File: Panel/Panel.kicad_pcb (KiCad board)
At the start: 2 copper layers, 30 x 128.5 mm, 7 parts

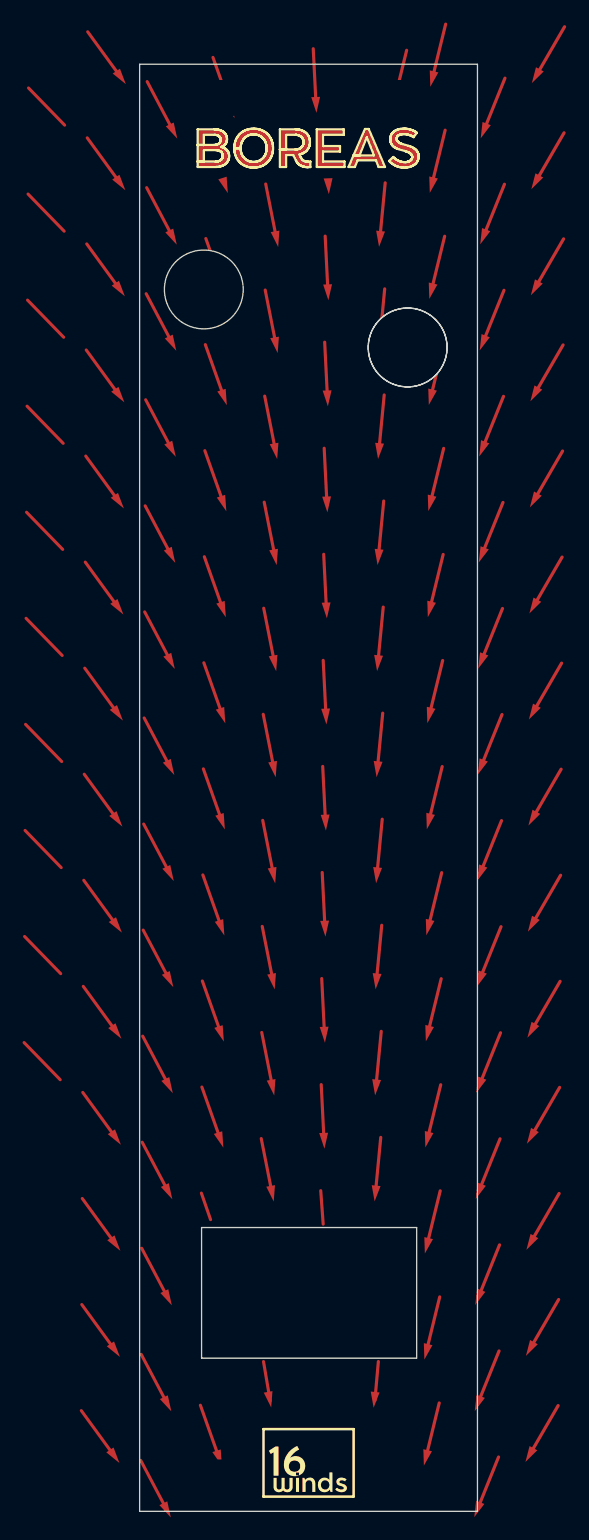
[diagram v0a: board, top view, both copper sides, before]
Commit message: Add logo to main board. Add readme for how to get images on pcb
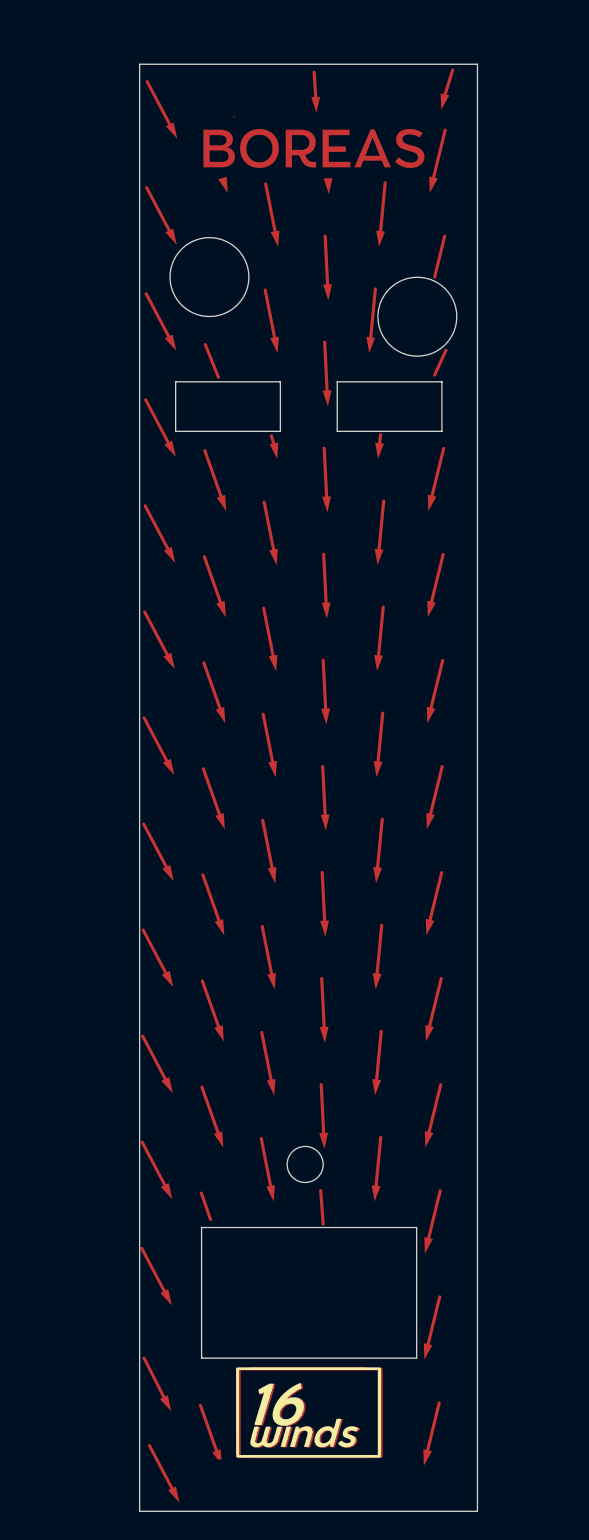
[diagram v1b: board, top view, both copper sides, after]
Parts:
- added Ref**: Val**, Footprints:16WindsLogo-96, F.Cu at (60.6, 157.6)
- moved ? 73.1 mm to (59.6, 132.2)
- moved REF** 2.86 mm to (69.5, 56.9)
- moved REF** 1.21 mm to (51.1, 53.4)
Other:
- outline, holes or cut-outs redrawn

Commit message: Remove two mounting holes. Add full board measurements.
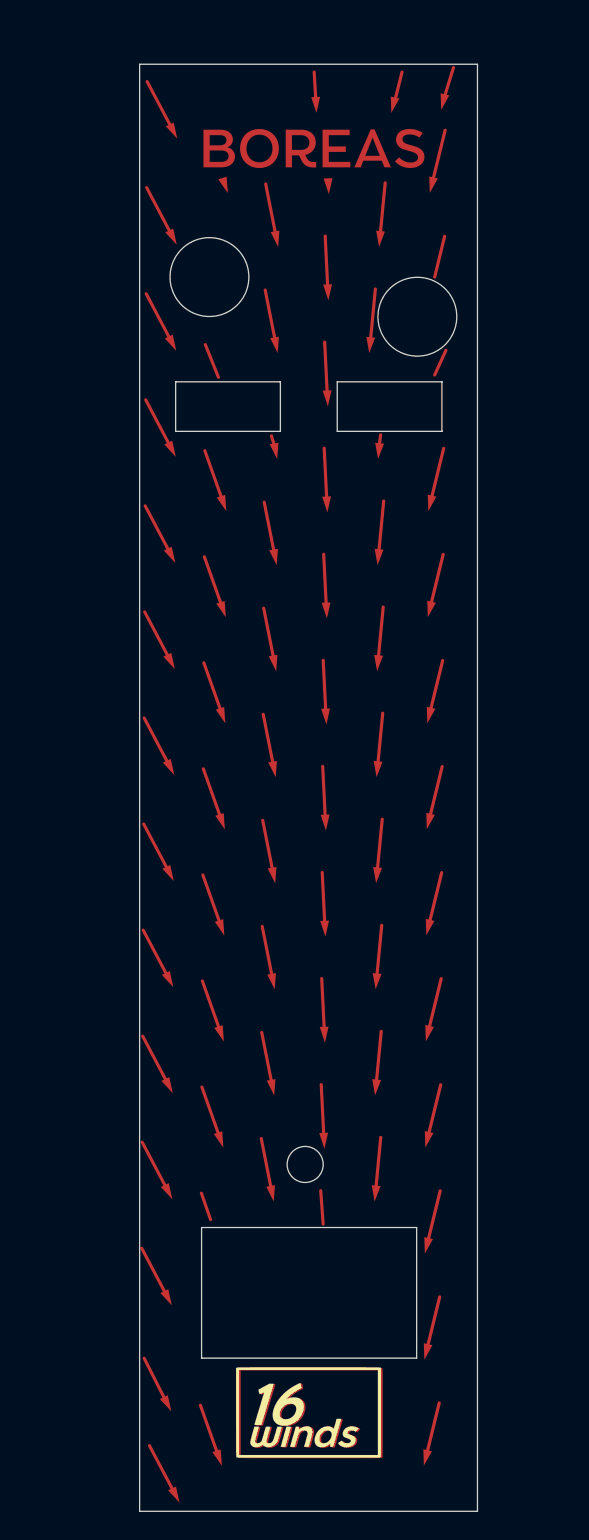
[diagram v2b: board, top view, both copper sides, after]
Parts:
- removed the ? at (67.4, 37.5)
- removed the ? at (52.4, 160.0)
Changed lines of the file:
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@@
     (pad "" np_thru_hole circle (at 0 0) (size 7 7) (drill 7) (layers *.Mask))
-  )
-  (footprint "" (layer "F.Cu")
-    (at 67.372 37.492)
-    (fp_text reference "" (at 0 0) (layer "F.SilkS")
-      (effects (font (size 1.27 1.27) (thickness 0.15)))
-    )
-    (fp_text value "" (at 0 0) (layer "F.SilkS")
-      (effects (font (size 1.27 1.27) (thickness 0.15)))
-    )
-    (pad "" np_thru_hole oval (at 0 0) (size 4.7 3.2) (drill oval 4.7 3.2) (layers F&B.Cu *.Mask))
-  )
-  (footprint "" (layer "F.Cu")
-    (at 52.372 159.992)
-    (fp_text reference "" (at 0 0) (layer "F.SilkS")
-      (effects (font (size 1.27 1.27) (thickness 0.15)))
-    )
-    (fp_text value "" (at 0 0) (layer "F.SilkS")
-      (effects (font (size 1.27 1.27) (thickness 0.15)))
-    )
-    (pad "" np_thru_hole oval (at 0 0) (size 4.7 3.2) (drill oval 4.7 3.2) (layers F&B.Cu *.Mask))
   )
   (gr_line (start 45.100405 130.215331) (end 47.231018 134.252143) (layer "F.Cu") (width 0.274499))
@@
   (gr_poly
     (pts
-      (xy 53.29391 39.270008)
-      (xy 52.446 38.048)
-      (xy 53.191368 37.811938)
-    ) (layer "F.Cu") (width 0) (fill solid))
-  (gr_poly
-    (pts
       (xy 71.314607 54.055165)
       (xy 70.595636 55.334218)
@@
     ) (layer "F.Cu") (width 0) (fill solid))
   (gr_line (start 71.740474 96.857058) (end 70.650936 101.307143) (layer "F.Cu") (width 0.281194))
-  (gr_line (start 72.672 34.992) (end 71.92723 37.417042) (layer "F.Cu") (width 0.281194))
+  (gr_line (start 68.172 35.192) (end 67.572 37.592) (layer "F.Cu") (width 0.281194))
   (gr_line (start 61.173318 87.426265) (end 61.400507 91.972598) (layer "F.Cu") (width 0.278962))
   (gr_line (start 66.371742 110.950774) (end 65.936746 115.493407) (layer "F.Cu") (width 0.281194))
@@
       (xy 52.425711 82.150519)
     ) (layer "F.Cu") (width 0) (fill solid))
+  (gr_line (start 72.744385 34.779479) (end 71.999615 37.204521) (layer "F.Cu") (width 0.281194))
   (gr_poly
     (pts
@@
       (effects (font (size 1 1) (thickness 0.15)))
     )
+    (format (units 3) (units_format 1) (precision 4))
+    (style (thickness 0.1) (arrow_length 1.27) (text_position_mode 0) (extension_height 0.58642) (extension_offset 0.5) keep_text_aligned)
+  )
+  (dimension (type orthogonal) (layer "Cmts.User")
+    (pts (xy 74.872 34.492) (xy 44.872 34.492))
+    (height -13.5)
+    (orientation 0)
+    (gr_text "30.0000 mm" (at 59.872 19.842) (layer "Cmts.User")
+      (effects (font (size 1 1) (thickness 0.15)))
+    )
